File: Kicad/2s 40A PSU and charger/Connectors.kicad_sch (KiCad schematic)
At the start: 20 parts, among them J1 Keystone 3579, J10 USB_C_Receptacle_USB2.0_16P, J11 1.27mm 4 pin socket, J2 JST XH-S Balance Plug, J3 Keystone 3579, J4 Keystone 3569, J5 Keystone 3569, J6 Keystone 3579, J7 Keystone 3579, J8 Keystone 3569, J9 Keystone 3569

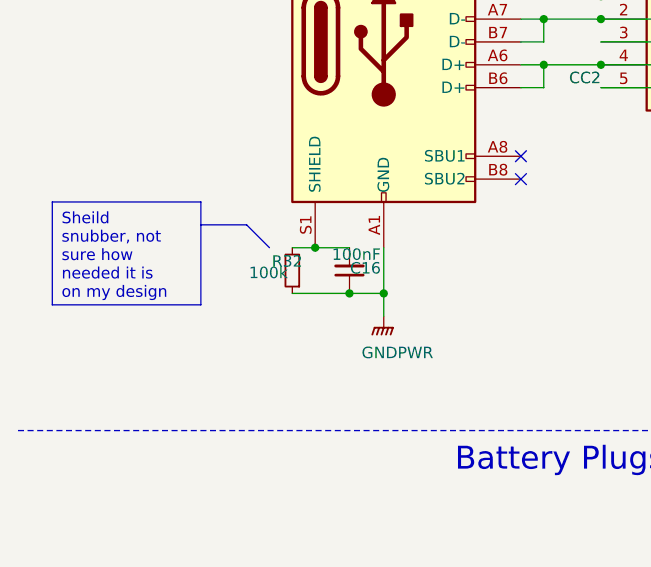
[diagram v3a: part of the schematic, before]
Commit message: Removed snubber from USB shield and connected direct to GND
This saves on components, and as far as good/bad RF practicalities go, many people are split on the practicality of it. I will go with the simpler method
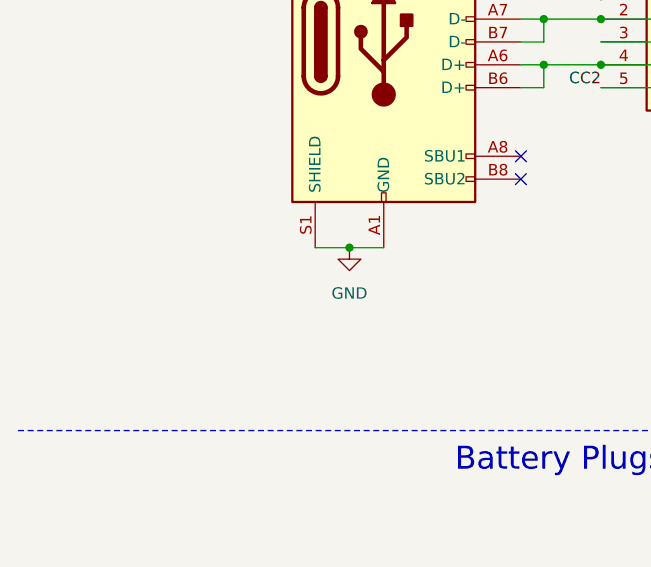
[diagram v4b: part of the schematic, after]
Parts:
- removed C16: 100nF, Capacitor_SMD:C_0402_1005Metric, symbol Device:C_Small
- removed R32: 100k, Resistor_SMD:R_0402_1005Metric, symbol Device:R_Small
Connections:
- net GND: now also J10.A1 (GND), J10.A12 (GND), J10.B1 (GND), J10.B12 (GND), J10.GND, J10.S1 (SHIELD)
- net GNDPWR: no longer J10.A1 (GND), J10.A12 (GND), J10.B1 (GND), J10.B12 (GND), J10.GND
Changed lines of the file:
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@@
 	)
 	(junction
-		(at 44.45 90.17)
-		(diameter 0)
-		(color 0 0 0 0)
-	)
-	(junction
 		(at 201.93 137.16)
 		(diameter 0)
@@
 	)
 	(junction
-		(at 52.07 95.25)
-		(diameter 0)
-		(color 0 0 0 0)
-	)
-	(junction
 		(at 201.93 95.25)
 		(diameter 0)
@@
 	)
 	(junction
-		(at 48.26 95.25)
+		(at 48.26 90.17)
 		(diameter 0)
 		(color 0 0 0 0)
@@
 		)
 	)
-	(polyline
-		(pts
-			(xy 36.83 87.63) (xy 39.37 90.17)
-		)
-		(stroke
-			(width 0)
-			(type default)
-		)
-	)
-	(wire
-		(pts
-			(xy 44.45 90.17) (xy 48.26 90.17)
-		)
-		(stroke
-			(width 0)
-			(type default)
-		)
-	)
-	(wire
-		(pts
-			(xy 41.91 90.17) (xy 44.45 90.17)
-		)
-		(stroke
-			(width 0)
-			(type default)
-		)
-	)
 	(wire
 		(pts
@@
 	(wire
 		(pts
-			(xy 201.93 151.13) (xy 203.2 151.13)
+			(xy 44.45 90.17) (xy 48.26 90.17)
 		)
 		(stroke
@@
 	(wire
 		(pts
-			(xy 201.93 109.22) (xy 201.93 113.03)
+			(xy 201.93 151.13) (xy 203.2 151.13)
 		)
 		(stroke
@@
 	(wire
 		(pts
-			(xy 203.2 147.32) (xy 201.93 147.32)
+			(xy 48.26 90.17) (xy 52.07 90.17)
 		)
 		(stroke
@@
 	(wire
 		(pts
-			(xy 52.07 97.79) (xy 52.07 95.25)
+			(xy 201.93 109.22) (xy 201.93 113.03)
 		)
 		(stroke
@@
 	(wire
 		(pts
-			(xy 201.93 105.41) (xy 201.93 109.22)
+			(xy 203.2 147.32) (xy 201.93 147.32)
 		)
 		(stroke
@@
 	(wire
 		(pts
-			(xy 59.69 168.91) (xy 68.58 168.91)
+			(xy 201.93 105.41) (xy 201.93 109.22)
 		)
 		(stroke
@@
 	(wire
 		(pts
-			(xy 207.01 49.53) (xy 213.36 49.53)
+			(xy 59.69 168.91) (xy 68.58 168.91)
 		)
 		(stroke
@@
 	(wire
 		(pts
-			(xy 201.93 137.16) (xy 201.93 140.97)
+			(xy 207.01 49.53) (xy 213.36 49.53)
 		)
 		(stroke
@@
 	(wire
 		(pts
-			(xy 48.26 95.25) (xy 52.07 95.25)
+			(xy 201.93 137.16) (xy 201.93 140.97)
 		)
 		(stroke
@@
 	(polyline
 		(pts
-			(xy 31.75 87.63) (xy 36.83 87.63)
-		)
-		(stroke
-			(width 0)
-			(type default)
-		)
-	)
-	(wire
-		(pts
-			(xy 41.91 95.25) (xy 48.26 95.25)
-		)
-		(stroke
-			(width 0)
-			(type default)
-		)
-	)
-	(polyline
-		(pts
 			(xy 135.89 11.43) (xy 135.89 198.12)
 		)
@@
 	(wire
 		(pts
-			(xy 52.07 95.25) (xy 52.07 90.17)
-		)
-		(stroke
-			(width 0)
-			(type default)
-		)
-	)
-	(wire
-		(pts
 			(xy 76.2 52.07) (xy 67.31 52.07)
 		)
@@
 		)
 	)
-	(text_box "Sheild snubber, not sure how needed it is on my design"
-		(exclude_from_sim no)
-		(at 15.24 85.09 0)
-		(size 16.51 11.43)
-		(stroke
-			(width 0)
-			(type default)
-		)
-		(fill
-			(type none)
-		)
-		(effects
-			(font
-				(size 1.27 1.27)
-			)
-			(justify left top)
-		)
-	)
 	(text "Outputs"
 		(exclude_from_sim no)
@@
 	(symbol
 		(lib_id "power:GNDPWR")
-		(at 52.07 97.79 0)
-		(unit 1)
-		(exclude_from_sim no)
-		(in_bom yes)
-		(on_board yes)
-		(dnp no)
-		(property "Reference" "#PWR014"
-			(at 52.07 102.87 0)
-			(effects
-				(font
-					(size 1.27 1.27)
-				)
-				(hide yes)
-			)
-		)
-		(property "Value" "GNDPWR"
-			(at 53.594 101.854 0)
-			(effects
-				(font
-					(size 1.27 1.27)
-				)
-			)
-		)
-		(property "Footprint" ""
-			(at 52.07 99.06 0)
-			(effects
-				(font
-					(size 1.27 1.27)
-				)
-				(hide yes)
-			)
-		)
-		(property "Datasheet" ""
-			(at 52.07 99.06 0)
-			(effects
-				(font
-					(size 1.27 1.27)
-				)
-				(hide yes)
-			)
-		)
-		(property "Description" "Power symbol creates a global label with name \"GNDPWR\" , global ground"
-			(at 52.07 97.79 0)
-			(effects
-				(font
-					(size 1.27 1.27)
-				)
-				(hide yes)
-			)
-		)
-		(pin "1"
-		)
-		(instances
-			(project "2s 40A PSU and charger"
-				(path "/eb3f183d-8bb1-43a5-a363-092ed67891e3/3a3003bc-8e40-4cd7-b859-421f37e4b48c"
-					(reference "#PWR014")
-					(unit 1)
-				)
-			)
-		)
-	)
-	(symbol
-		(lib_id "power:GNDPWR")
 		(at 88.9 55.88 0)
 		(unit 1)
@@
 	)
 	(symbol
-		(lib_id "Device:C_Small")
-		(at 48.26 92.71 180)
-		(unit 1)
-		(exclude_from_sim no)
-		(in_bom yes)
-		(on_board yes)
-		(dnp no)
-		(property "Reference" "C16"
-			(at 50.038 92.456 0)
-			(effects
-				(font
-					(size 1.27 1.27)
-				)
-			)
-		)
-		(property "Value" "100nF"
-			(at 49.022 90.932 0)
-			(effects
-				(font
-					(size 1.27 1.27)
-				)
-			)
-		)
-		(property "Footprint" "Capacitor_SMD:C_0402_1005Metric"
-			(at 48.26 92.71 0)
-			(effects
-				(font
-					(size 1.27 1.27)
-				)
-				(hide yes)
-			)
-		)
-		(property "Datasheet" "~"
-			(at 48.26 92.71 0)
-			(effects
-				(font
-					(size 1.27 1.27)
-				)
-				(hide yes)
-			)
-		)
-		(property "Description" "Unpolarized capacitor, small symbol"
-			(at 48.26 92.71 0)
-			(effects
-				(font
-					(size 1.27 1.27)
-				)
-				(hide yes)
-			)
-		)
-		(pin "2"
-		)
-		(pin "1"
-		)
-		(instances
-			(project "2s 40A PSU and charger"
-				(path "/eb3f183d-8bb1-43a5-a363-092ed67891e3/3a3003bc-8e40-4cd7-b859-421f37e4b48c"
-					(reference "C16")
-					(unit 1)
-				)
-			)
-		)
-	)
-	(symbol
 		(lib_id "power:GND")
 		(at 123.19 77.47 0)
@@
 	)
 	(symbol
-		(lib_id "Device:R_Small")
-		(at 41.91 92.71 180)
-		(unit 1)
-		(exclude_from_sim no)
-		(in_bom yes)
-		(on_board yes)
-		(dnp no)
-		(property "Reference" "R32"
-			(at 39.624 91.694 0)
-			(effects
-				(font
-					(size 1.27 1.27)
-				)
-				(justify right)
-			)
-		)
-		(property "Value" "100k"
-			(at 37.084 92.964 0)
-			(effects
-				(font
-					(size 1.27 1.27)
-				)
-				(justify right)
-			)
-		)
-		(property "Footprint" "Resistor_SMD:R_0402_1005Metric"
-			(at 41.91 92.71 0)
-			(effects
-				(font
-					(size 1.27 1.27)
-				)
-				(hide yes)
-			)
-		)
-		(property "Datasheet" "~"
-			(at 41.91 92.71 0)
-			(effects
-				(font
-					(size 1.27 1.27)
-				)
-				(hide yes)
-			)
-		)
-		(property "Description" "Resistor, small symbol"
-			(at 41.91 92.71 0)
-			(effects
-				(font
-					(size 1.27 1.27)
-				)
-				(hide yes)
-			)
-		)
-		(pin "1"
-		)
-		(pin "2"
-		)
-		(instances
-			(project "2s 40A PSU and charger"
-				(path "/eb3f183d-8bb1-43a5-a363-092ed67891e3/3a3003bc-8e40-4cd7-b859-421f37e4b48c"
-					(reference "R32")
-					(unit 1)
-				)
-			)
-		)
-	)
-	(symbol
 		(lib_id "Connector_Generic:Conn_01x03")
 		(at 74.93 166.37 0)
@@
 					(unit 1)
 				)
+			)
+		)
+	)
+	(symbol
+		(lib_id "power:GND")
+		(at 48.26 90.17 0)
+		(unit 1)
+		(exclude_from_sim no)
+		(in_bom yes)
+		(on_board yes)
+		(dnp no)
+		(fields_autoplaced yes)
+		(property "Reference" "#PWR02"
+			(at 48.26 96.52 0)
+			(effects
+				(font
+					(size 1.27 1.27)
+				)
+				(hide yes)
+			)
+		)
+		(property "Value" "GND"
+			(at 48.26 95.25 0)
+			(effects
+				(font
+					(size 1.27 1.27)
+				)
+			)
+		)
+		(property "Footprint" ""
+			(at 48.26 90.17 0)
+			(effects
+				(font
+					(size 1.27 1.27)
+				)
+				(hide yes)
+			)
+		)
+		(property "Datasheet" ""
+			(at 48.26 90.17 0)
+			(effects
+				(font
+					(size 1.27 1.27)
+				)
+				(hide yes)
+			)
+		)
+		(property "Description" "Power symbol creates a global label with name \"GND\" , ground"
+			(at 48.26 90.17 0)
+			(effects
+				(font
+					(size 1.27 1.27)
+				)
+				(hide yes)
+			)
+		)
+		(pin "1"
+		)
+		(instances
+			(project "2s 40A PSU and charger"
+				(path "/eb3f183d-8bb1-43a5-a363-092ed67891e3/3a3003bc-8e40-4cd7-b859-421f37e4b48c"
+					(reference "#PWR02")
+					(unit 1)
+				)

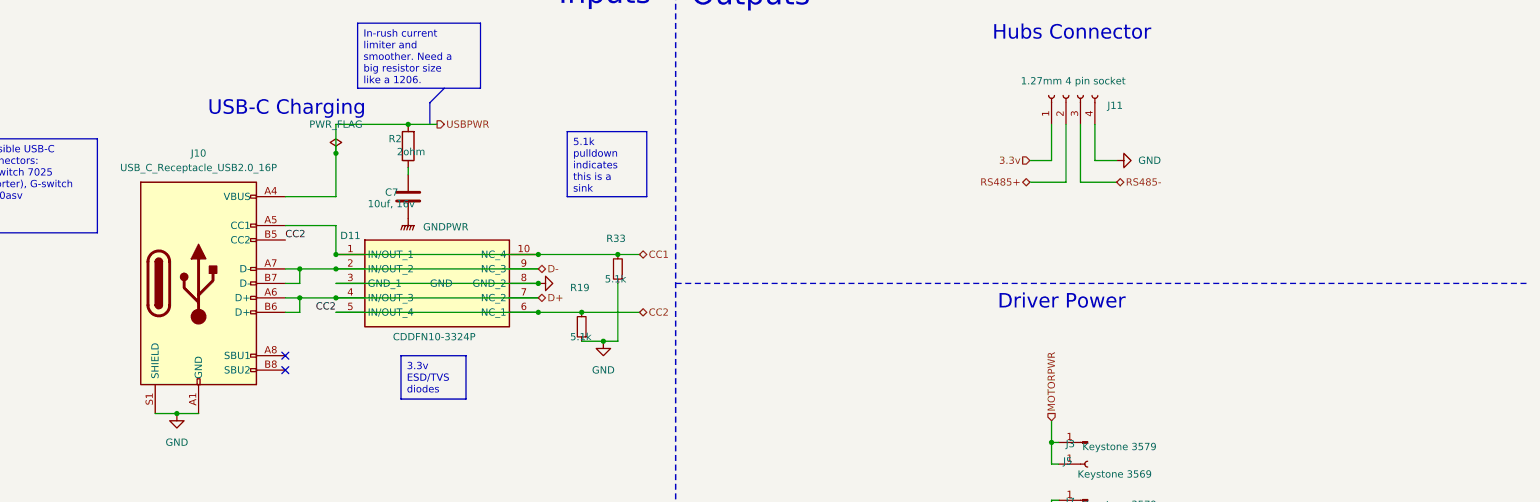
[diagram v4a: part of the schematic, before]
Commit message: Finished Layout of PSU
Gosh, this has taken a long time on and off, almost 2 months!
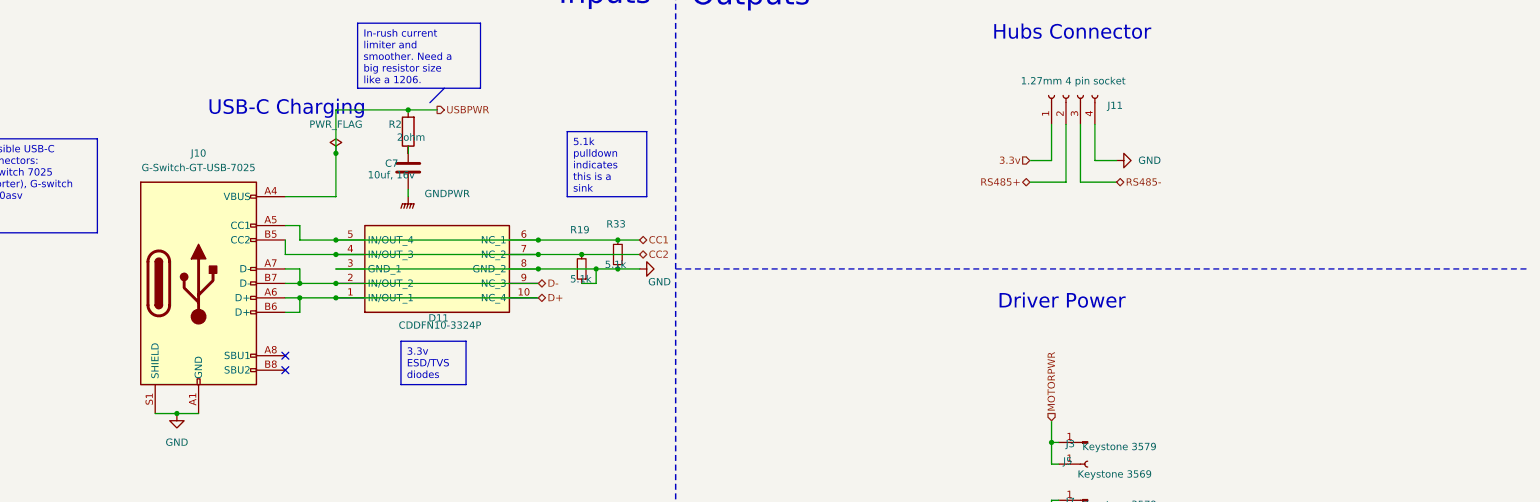
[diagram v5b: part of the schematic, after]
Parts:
- J10: value USB_C_Receptacle_USB2.0_16P -> G-Switch-GT-USB-7025
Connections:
- net CC1: now also D11.5 (IN/OUT_4), D11.6 (NC_1); no longer D11.1 (IN/OUT_1), D11.10 (NC_4)
- net CC2: now also D11.4 (IN/OUT_3), D11.7 (NC_2); no longer D11.5 (IN/OUT_4), D11.6 (NC_1)
- net D+: now also D11.1 (IN/OUT_1), D11.10 (NC_4); no longer D11.4 (IN/OUT_3), D11.7 (NC_2)
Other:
- moved on the sheet: C7, D11, R19, R2, R33

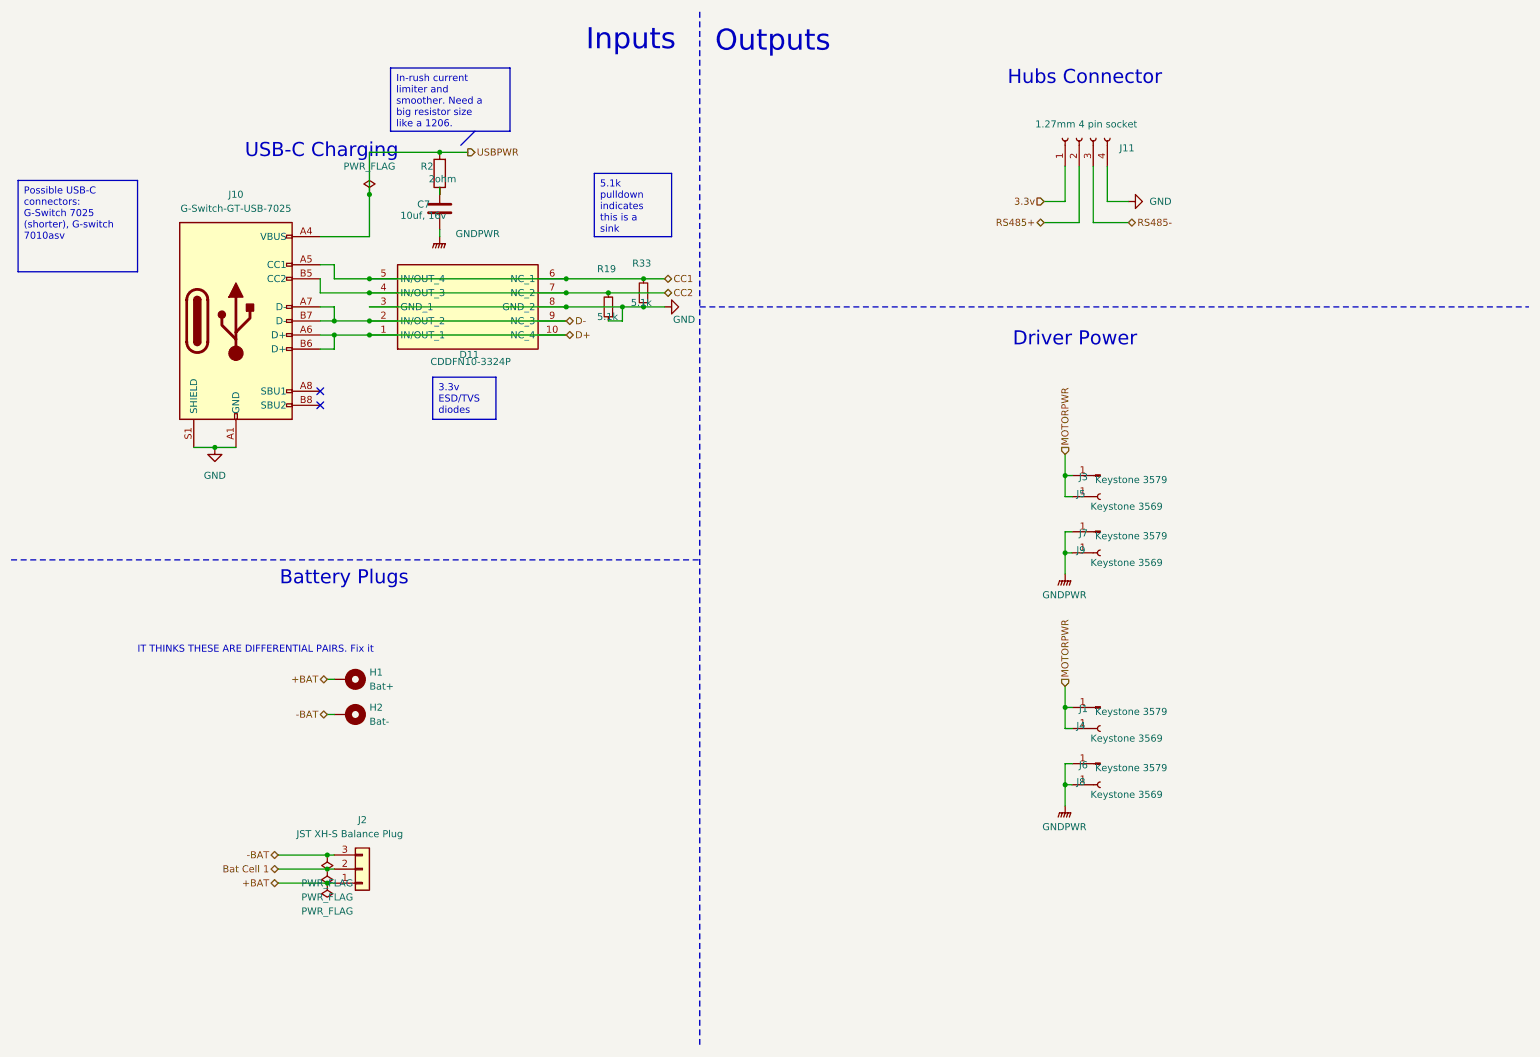
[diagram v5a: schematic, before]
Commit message: Combined separate ground planes
I now have one solid ground plane. There really was no point in having separate ground planes EXCEPT for keeping the high current return path away from the MCU and sense lines. I have added a keepout zone on the top half, to split to keep the high current return from going into the MCU section, but that is it.
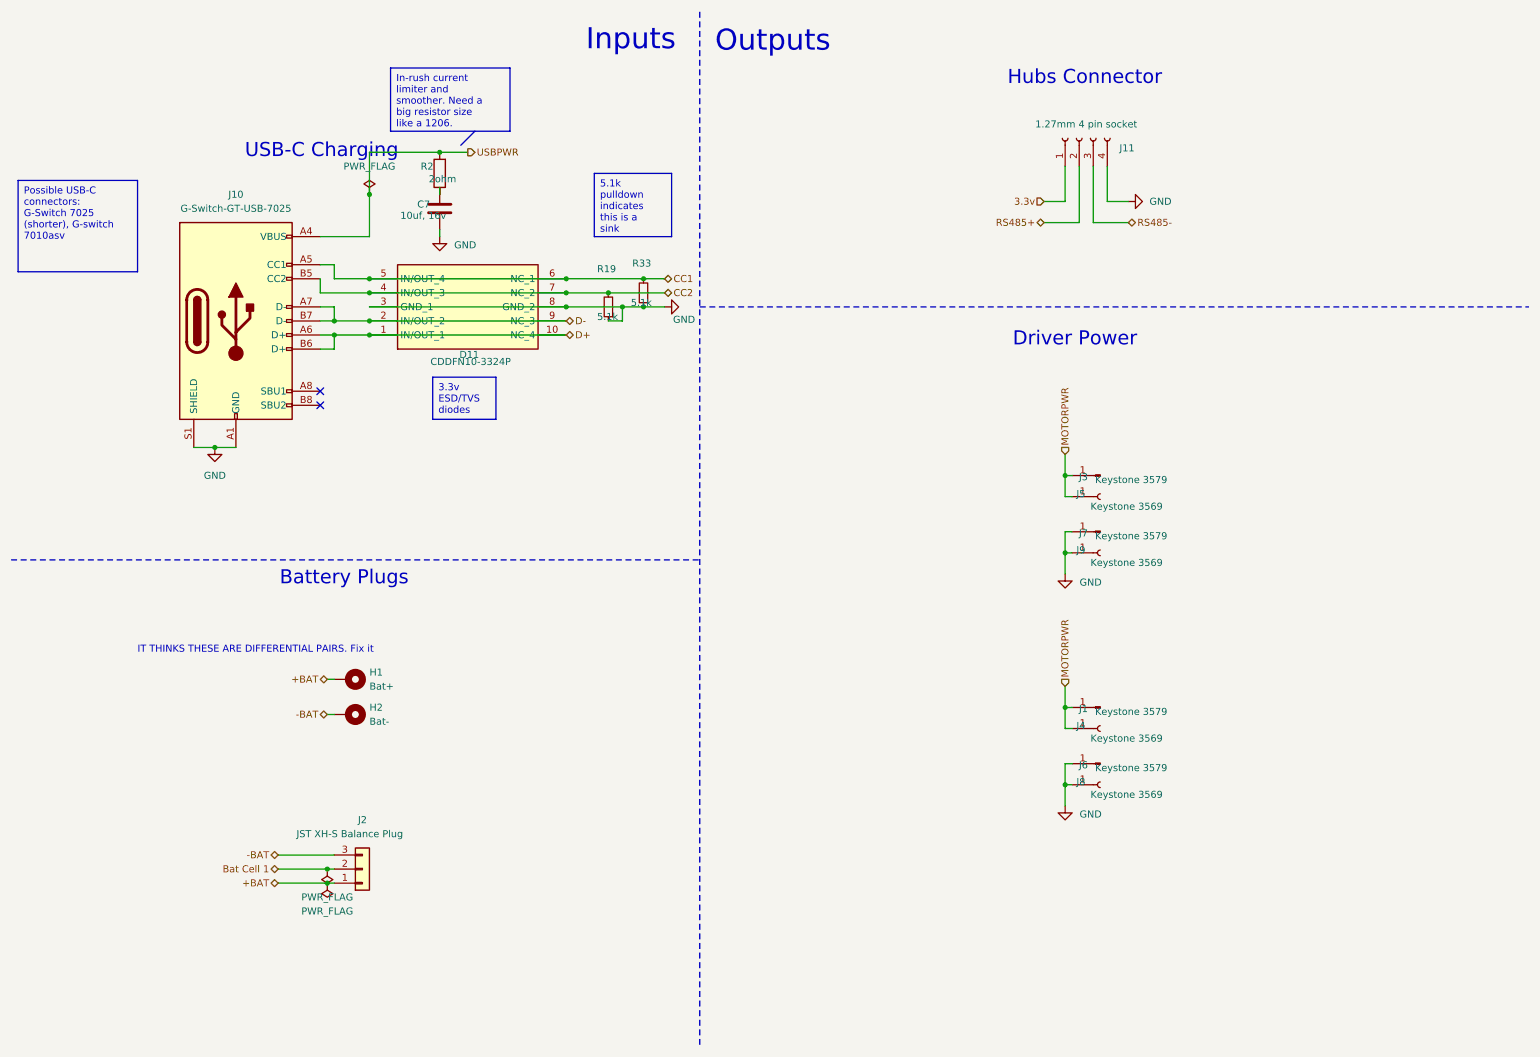
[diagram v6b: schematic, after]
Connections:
- net GNDPWR is gone; now on net GND: C7.2, J6.1 (Pin_1), J7.1 (Pin_1), J8.1 (Pin_1), J9.1 (Pin_1)

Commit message: Finished routing PSU
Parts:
- J10: footprint Connector_USB:USB_C_Receptacle_G-Switch_GT-USB-7025 -> custom_Connector:USB_C_G-Switch_GT-USB-7025-JLCPCBv
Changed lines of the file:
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@@
 			)
 		)
-		(property "Footprint" "Connector_USB:USB_C_Receptacle_G-Switch_GT-USB-7025"
+		(property "Footprint" "custom_Connector:USB_C_G-Switch_GT-USB-7025-JLCPCBv"
 			(at 55.88 67.31 0)
 			(effects
